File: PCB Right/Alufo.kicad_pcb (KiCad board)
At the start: 2 copper layers, 282.6 x 90.9 mm, 95 parts, among them J2 USB_C_Receptacle_USB2.0_16P_2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, J4 USB_C_Receptacle_USB2.0_16P_2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, J6 SolderHole, K11 PG1350, K12 PG1350, K13 PG1350, K14 PG1350, K15 PG1350, K16 PG1350, K21 PG1350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

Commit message: Add cutout in middle layer for solder jump
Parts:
- J6: footprint TestPoint:TestPoint_THTPad_D2.5mm_Drill1.2mm -> Project Library:TestPoint_THTPad_D2.5mm_Drill1.2mm
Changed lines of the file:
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@@
 		)
 	)
-	(footprint "TestPoint:TestPoint_THTPad_D2.5mm_Drill1.2mm"
+	(footprint "Project Library:TestPoint_THTPad_D2.5mm_Drill1.2mm"
 		(layer "F.Cu")
 		(at 95.25 65.567997)
@@
 			)
 		)
-		(property "Footprint" "TestPoint:TestPoint_THTPad_D2.5mm_Drill1.2mm"
+		(property "Footprint" "Project Library:TestPoint_THTPad_D2.5mm_Drill1.2mm"
 			(at 0 0 0)
 			(unlocked yes)
@@
 			(layer "F.CrtYd")
 		)
+		(fp_circle
+			(center 0 0)
+			(end 1.45 0)
+			(stroke
+				(width 0.12)
+				(type solid)
+			)
+			(fill none)
+			(layer "User.2")
+		)
 		(fp_text user "${REFERENCE}"

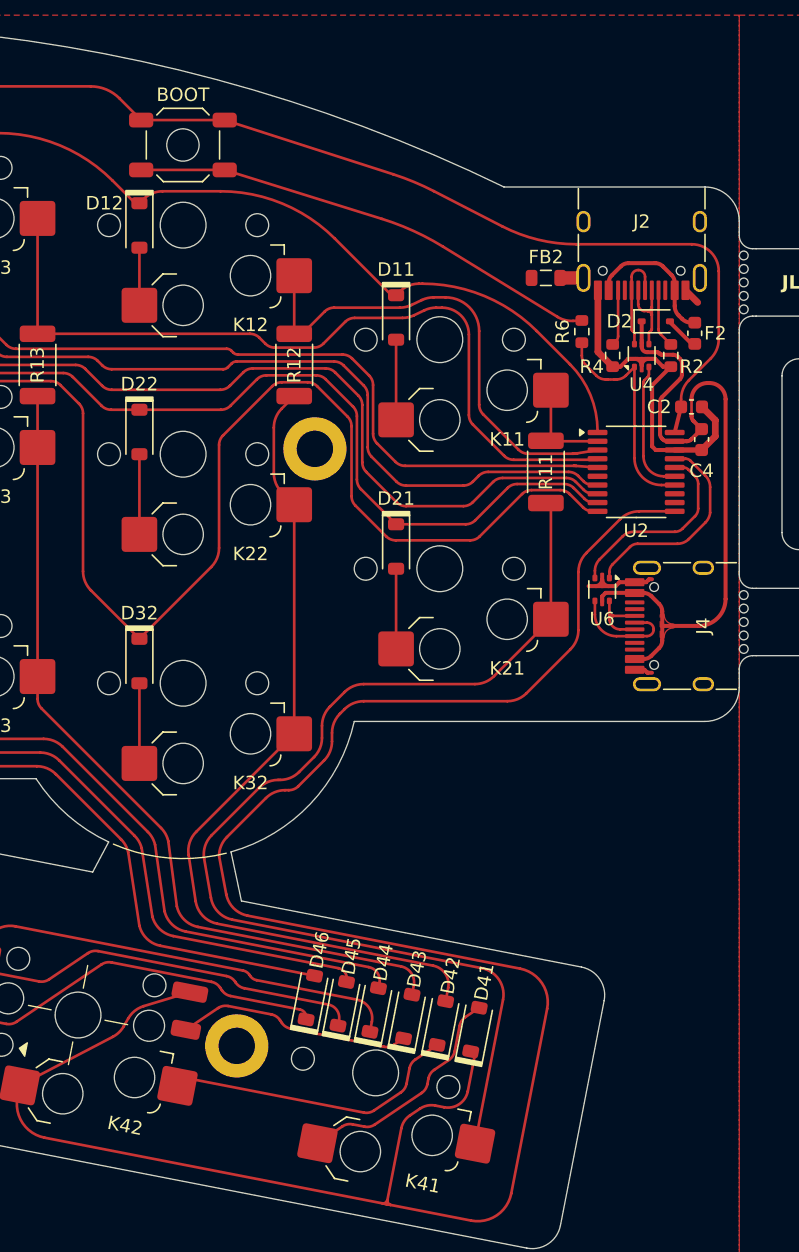
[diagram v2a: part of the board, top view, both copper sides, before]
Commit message: Further library name corrections in schematic; update PCB
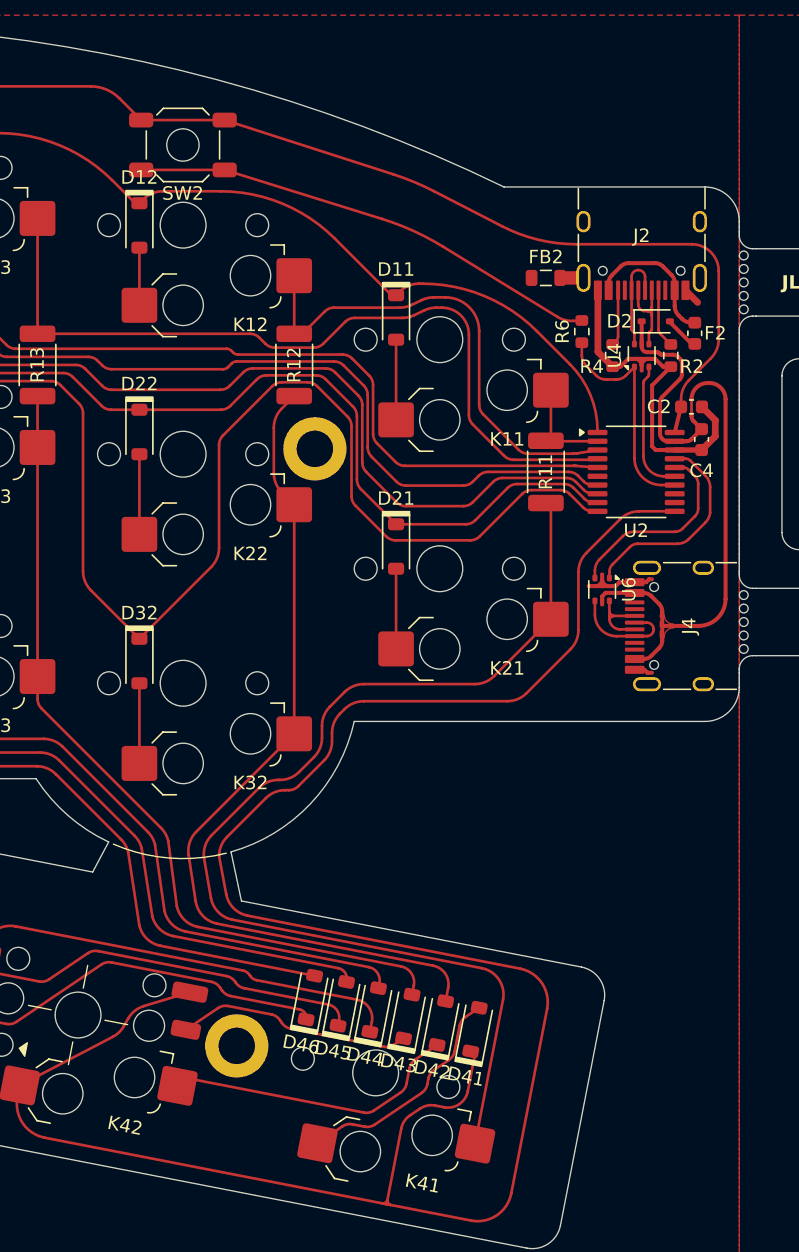
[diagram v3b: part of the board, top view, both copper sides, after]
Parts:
- D11, D12, D13, D14, D15, D16, D21, D22, D23, D24, D25, D26, D32, D33, D34, D35: footprint Project Library:D_SOD-123_Mod -> Project_Library:D_SOD-123_Mod
- D41, D42, D43, D44, D45, D46: footprint Project Library:D_SOD-123 -> Project_Library:D_SOD-123
- H1, H2, H4, H5: footprint Project Library:MountingHole_2.2mm_M2_SMD_Solder_Nut -> Project_Library:MountingHole_2.2mm_M2_SMD_Solder_Nut
- H11, H12, H13, H14: footprint Project Library:Mousebites -> Project_Library:Mousebites
- H3: footprint Project Library:MountingHole_2.2mm_M2_SMD_Solder_Nut_Pad -> Project_Library:MountingHole_2.2mm_M2_SMD_Solder_Nut_Pad
- J2, J4: footprint Project Library:USB_C_Receptacle_HRO_TYPE-C-31-M-12 -> Project_Library:USB_C_Receptacle_HRO_TYPE-C-31-M-12
- J6: footprint Project Library:TestPoint_THTPad_D2.5mm_Drill1.2mm -> Project_Library:TestPoint_THTPad_D2.5mm_Drill1.2mm
- K11, K12, K13, K14, K15, K16, K21, K22, K23, K24, K25, K26, K32, K33, K34, K35: footprint Project Library:SW_choc_v1_HS_CPG135001S30_1layer_1u -> Project_Library:SW_choc_v1_HS_CPG135001S30_1layer_1u
- K41: footprint Project Library:SW_choc_v1_HS_CPG135001S30_1layer_1.5u -> Project_Library:SW_choc_v1_HS_CPG135001S30_1layer_1.5u
- K42: footprint Project Library:SW_choc_v1_HS_nav_CPG135001S30_SKQUCAA010_1layer_1u_1 -> Project_Library:SW_choc_v1_HS_nav_CPG135001S30_SKQUCAA010_1layer_1u_1
- L2: footprint Project Library:LED_0805_2012Metric_Mod -> Project_Library:LED_0805_2012Metric_Mod
- NT2: footprint Project Library:NetTie-2_SMD_Pad0.2mm -> Project_Library:NetTie-2_SMD_Pad0.2mm
- PK11, PK12, PK13, PK14, PK15, PK16, PK21, PK22, PK23, PK24, PK25, PK26, PK32, PK33, PK34, PK35, PK42: footprint Project Library:SW_choc_v1_Plate_CPG135001S30_1u -> Project_Library:SW_choc_v1_Plate_CPG135001S30_1u
- PK41: footprint Project Library:SW_choc_v1_Plate_CPG135001S30_1.5u -> Project_Library:SW_choc_v1_Plate_CPG135001S30_1.5u
- SW2: footprint Project Library:SW_SPST_SKQG_WithStem -> Project_Library:SW_SPST_SKQG_WithStem
- U4, U6: footprint Project Library:SOT-666_Mod -> Project_Library:SOT-666_Mod

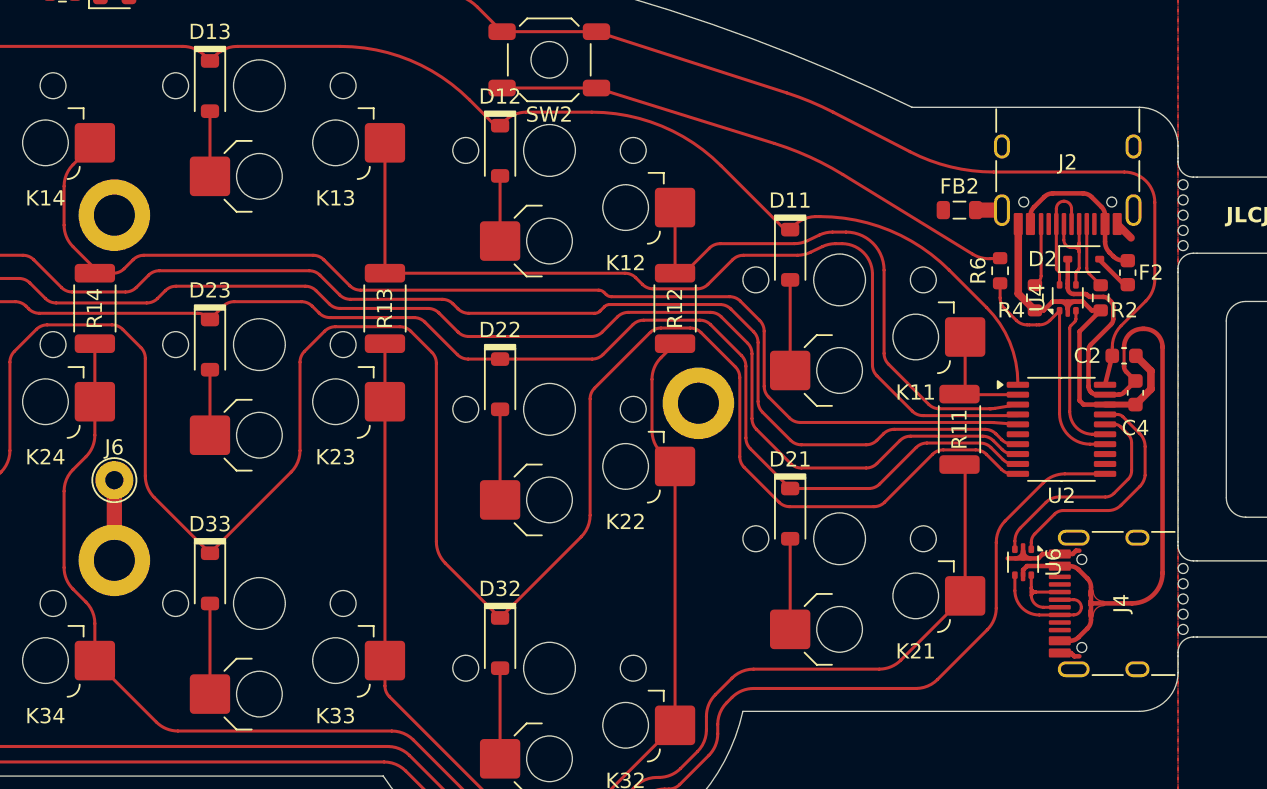
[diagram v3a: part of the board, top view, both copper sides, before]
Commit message: Update right side
Also add outline for middle layer to new USB port footprint (although it won’t be right.
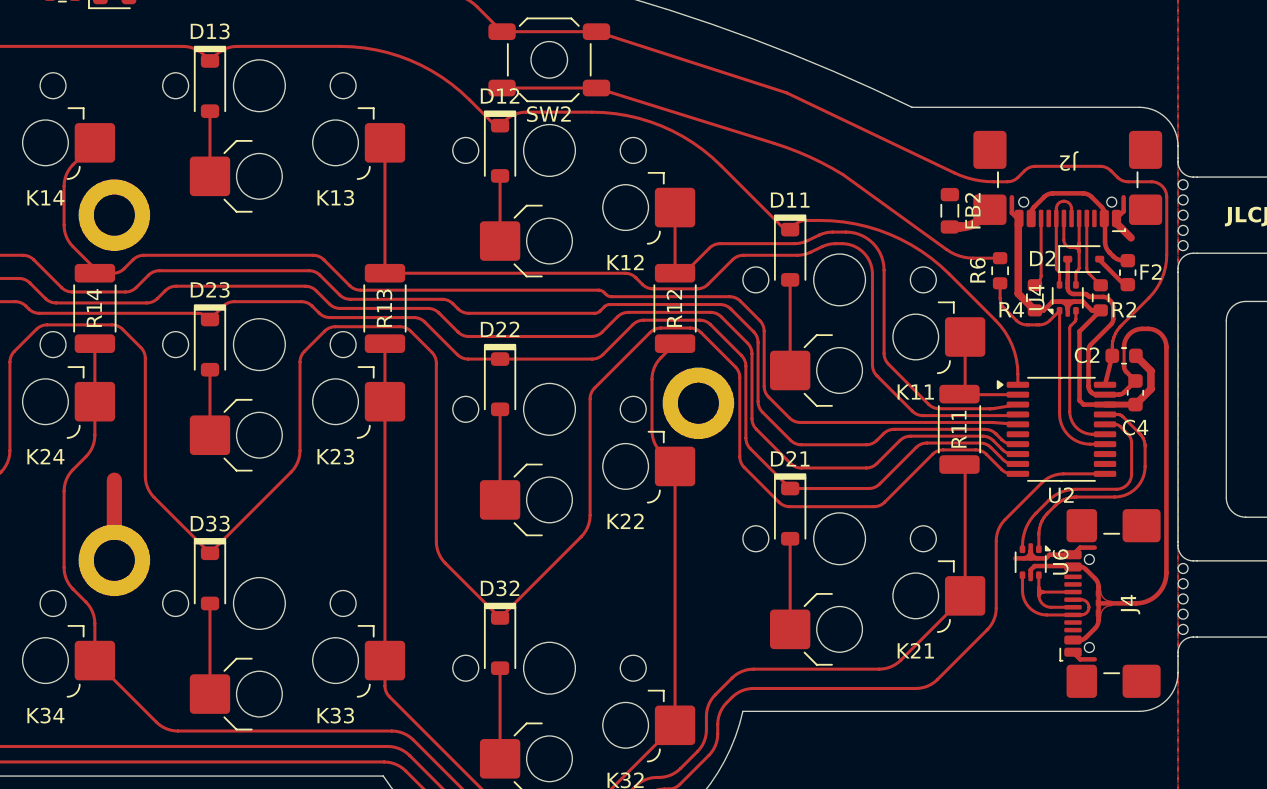
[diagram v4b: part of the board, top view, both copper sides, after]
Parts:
- removed J6: SolderHole, Project_Library:TestPoint_THTPad_D2.5mm_Drill1.2mm
- H3: footprint Project_Library:MountingHole_2.2mm_M2_SMD_Solder_Nut_Pad -> Project_Library:MountingHole_2.2mm_M2_SMD_Solder_Nut
- J2, J4: footprint Project_Library:USB_C_Receptacle_HRO_TYPE-C-31-M-12 -> Project_Library:USB_C_Receptacle_GCT_USB4110
- moved FB2 0.64 mm to (150.1, 47.9), turned to 90 degrees
- moved J4 0.50 mm to (161.9, 73.7)
- moved U6 0.50 mm to (155.4, 71.0)
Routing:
- net Shield: track 5.27 -> 0.00 mm
- net (no net): track 0.00 -> 5.27 mm
- net GND: track 29.9 -> 34.0 mm
- net +3V3: track 84.0 -> 85.7 mm
- net Net-(FB2-Pad1): track 1.40 -> 3.01 mm
